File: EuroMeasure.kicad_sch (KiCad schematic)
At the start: 33 parts, among them SW901 SW_DIP_x04, SW902 RST, U901 AZ1117-3V3, U902 STM32G030CxT, Y901 16MHz

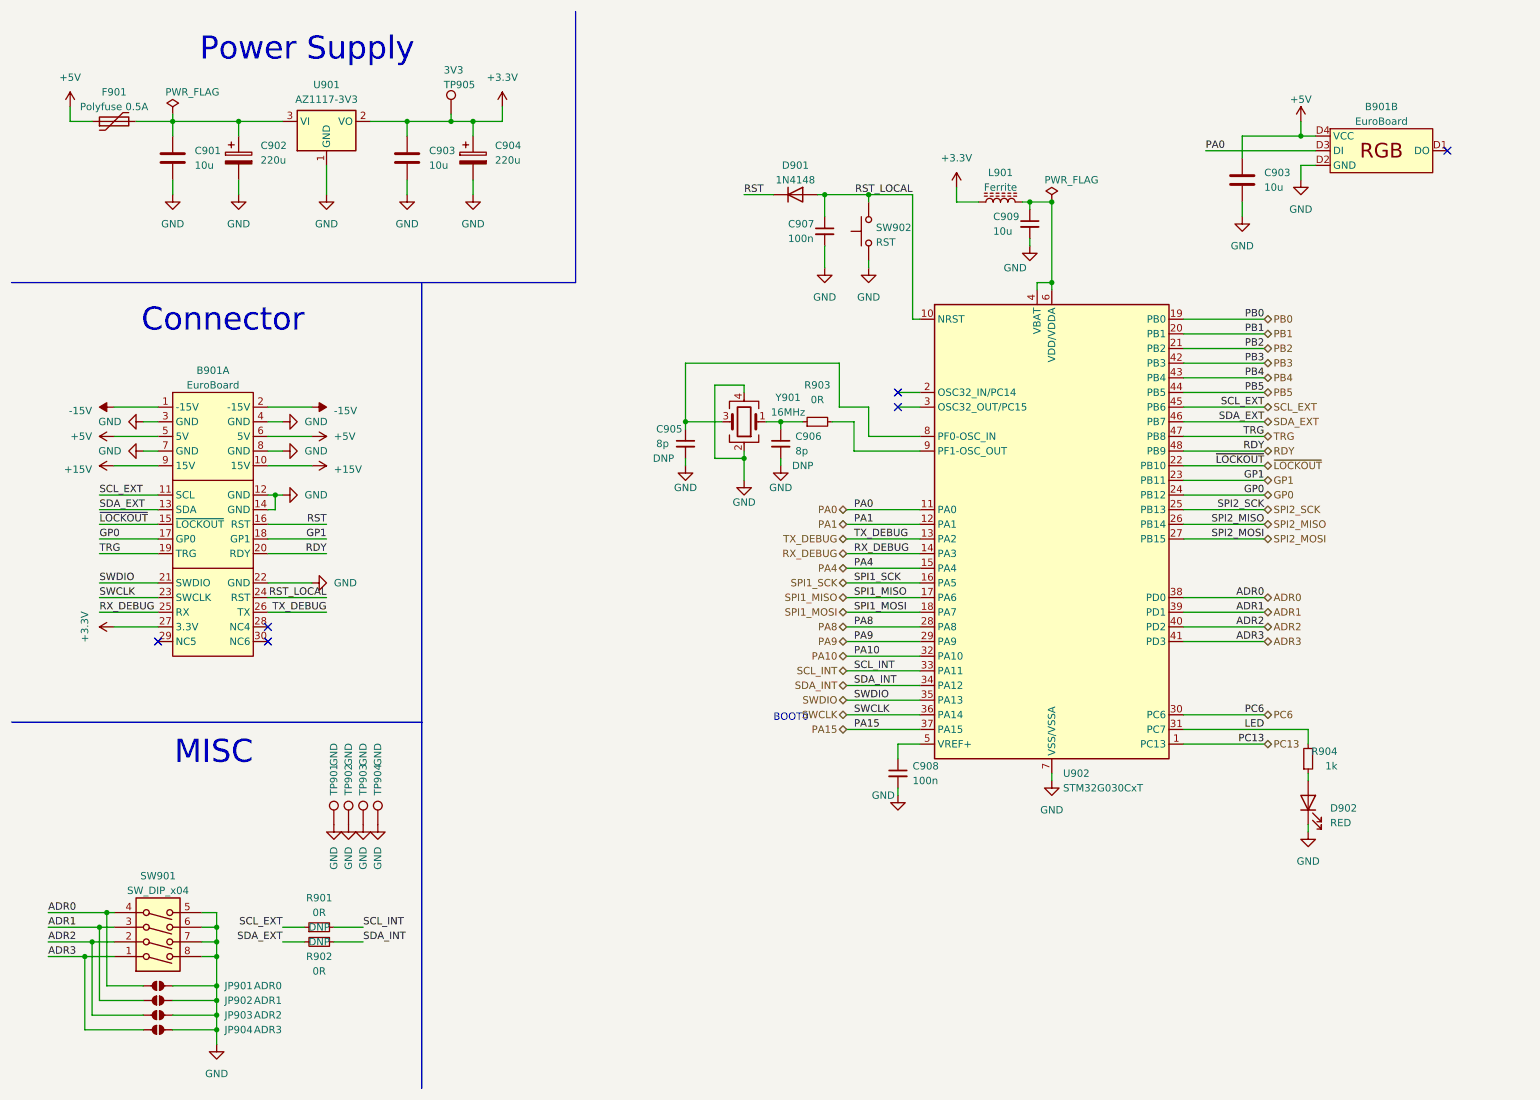
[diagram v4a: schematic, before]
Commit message: Revised labelling
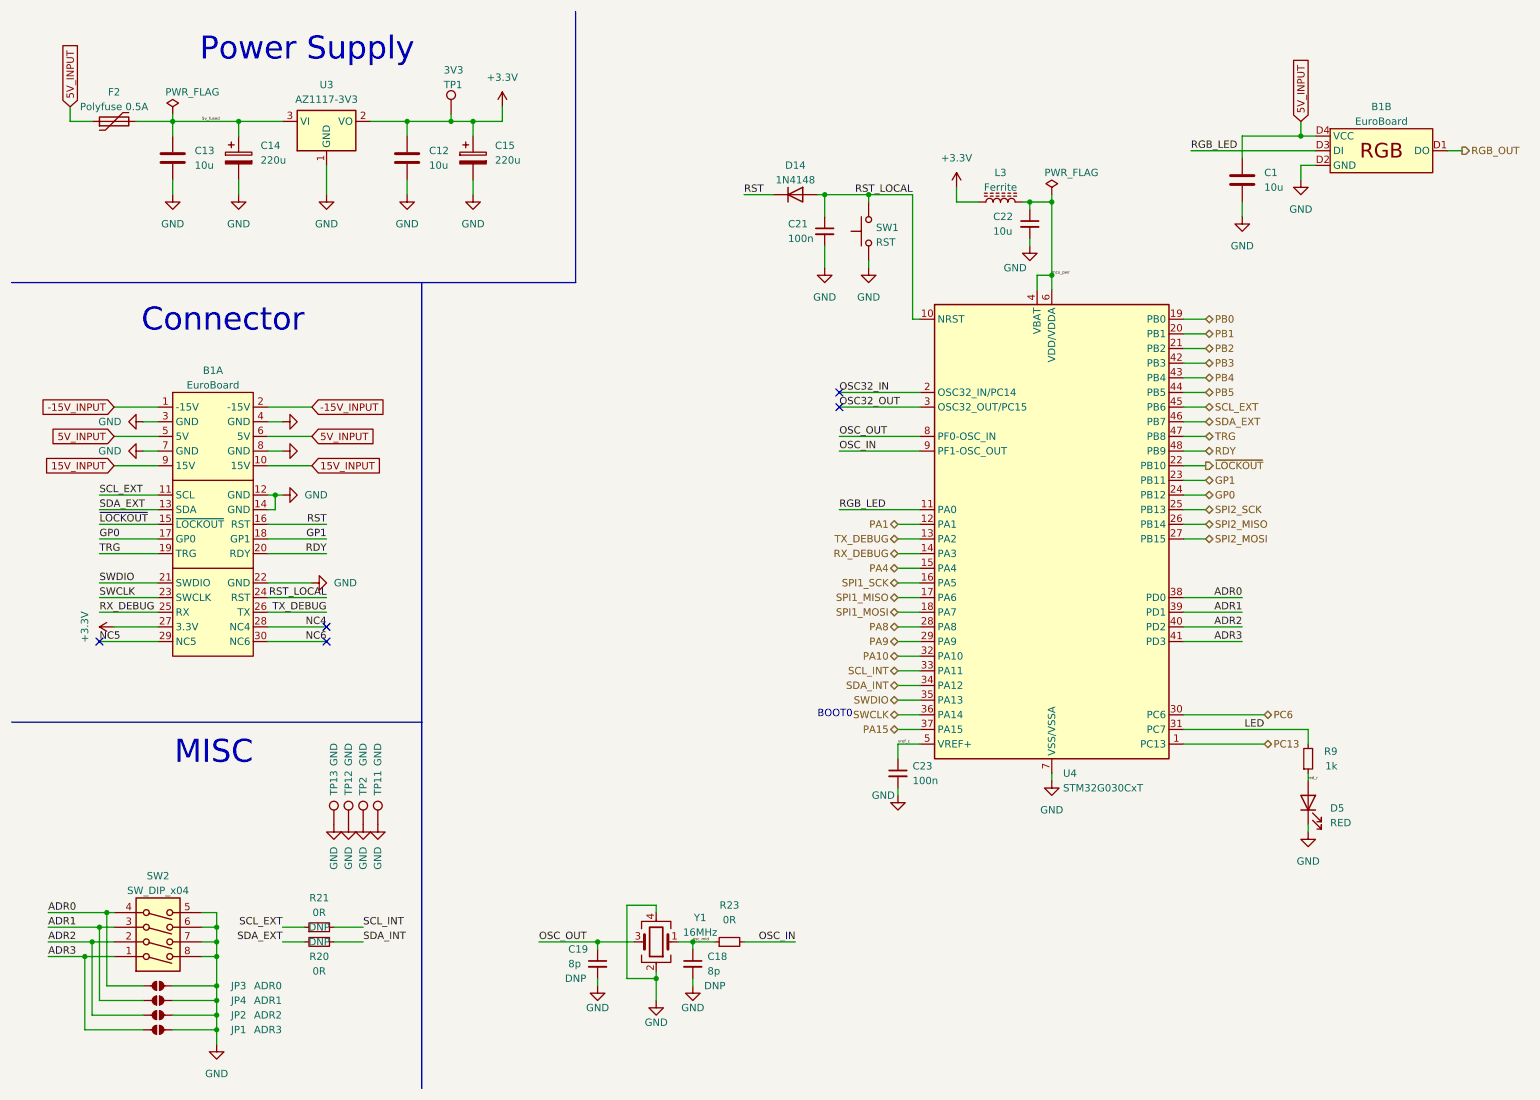
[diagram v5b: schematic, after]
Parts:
- renumbered B901 to B1, C903 to C1, C903 to C12, C901 to C13, C902 to C14, C904 to C15, C906 to C18, C905 to C19, C907 to C21, C909 to C22, C908 to C23, D901 to D14, D902 to D5, F901 to F2, JP904 to JP1, JP903 to JP2, JP901 to JP3, JP902 to JP4, L901 to L3, R902 to R20, R901 to R21, R903 to R23, R904 to R9, SW902 to SW1, SW901 to SW2, TP905 to TP1, TP904 to TP11, TP902 to TP12, TP901 to TP13, TP903 to TP2, U901 to U3, U902 to U4, Y901 to Y1
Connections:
- net mcu_pwr: now reaches C22.1, L3.2, U4.4 (VBAT), U4.6 (VDD/VDDA)
- net osc_mid: now reaches C18.1, R23.1, Y1.1
- net OSC_OUT: now reaches C19.1, U4.8 (PF0-OSC_IN), Y1.3
- net 5v_fused: now reaches C13.1, C14.1, F2.2, U3.3 (VI)
- net led_r: now reaches D5.2 (A), R9.1
- net OSC_IN: now reaches R23.2, U4.9 (PF1-OSC_OUT)
- net RGB_OUT: now reaches B1.D1 (DO)
- net NC4: now reaches B1.28 (NC4)
- net NC5: now reaches B1.29 (NC5)
- net NC6: now reaches B1.30 (NC6)
- net OSC32_IN: now reaches U4.2 (OSC32_IN/PC14)
- net OSC32_OUT: now reaches U4.3 (OSC32_OUT/PC15)
- net vref_c: now reaches C23.1, U4.5 (VREF+)
- net +15V renamed 15V_INPUT
- net +5V renamed 5V_INPUT
- net -15V renamed -15V_INPUT
- net PA0 renamed RGB_LED
- no-connect marks 6 -> 5
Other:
- title: (none) -> EuroMeasure-HVPSU
- moved on the sheet: C18, C19, R23, Y1

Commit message: Cleaned up schematic
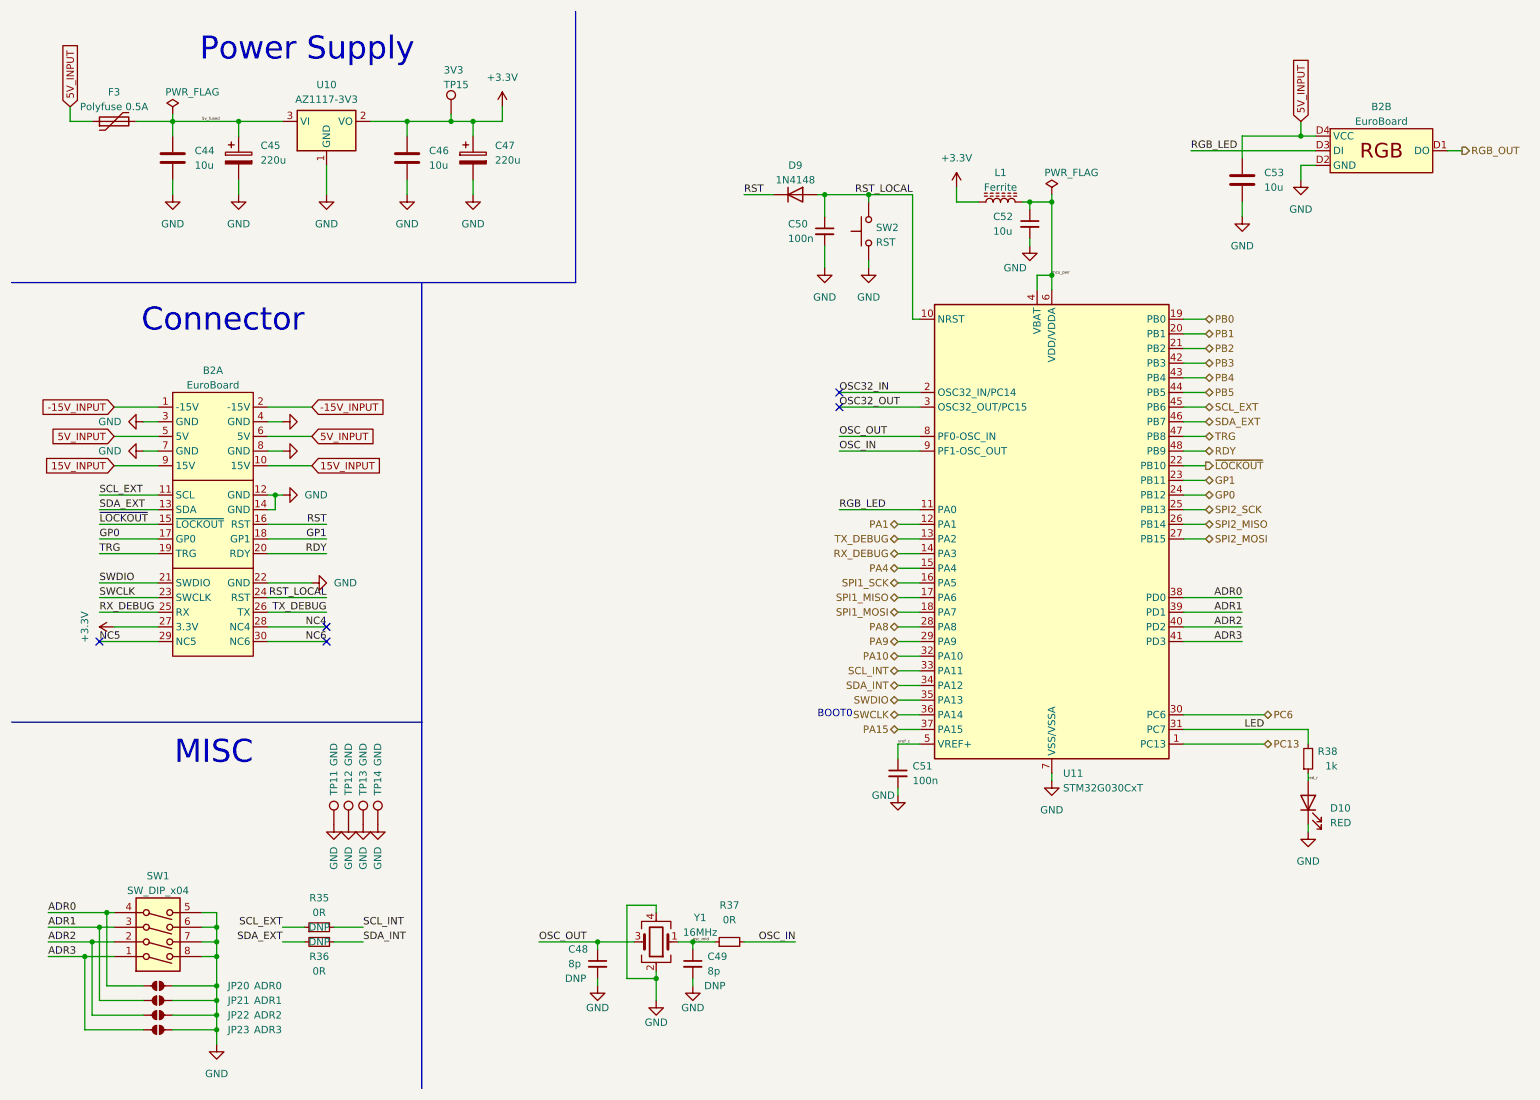
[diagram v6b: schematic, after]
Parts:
- renumbered B1 to B2, C13 to C44, C14 to C45, C12 to C46, C15 to C47, C19 to C48, C18 to C49, C21 to C50, C23 to C51, C22 to C52, C1 to C53, D5 to D10, D14 to D9, F2 to F3, JP3 to JP20, JP4 to JP21, JP2 to JP22, JP1 to JP23, L3 to L1, R21 to R35, R20 to R36, R23 to R37, R9 to R38, SW2 to SW1, SW1 to SW2, TP13 to TP11, TP2 to TP13, TP11 to TP14, TP1 to TP15, U3 to U10, U4 to U11

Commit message: Cleaned up PCB
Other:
- moved on the sheet: B2B, C48, C49, C53, R37, Y1
